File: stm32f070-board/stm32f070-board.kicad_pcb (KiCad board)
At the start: 2 copper layers, 39 parts, among them J1 USB_B_Micro, J2 USB_B_Micro, J3 Conn_01x05_Male, SW1 SW_DPDT_x2, SW2 SW_Push, SW3 SW_Push, U1 CH340G, U2 STM32F070F6P6, U3 MCP9700AT-ETT, U4 Si7055-A20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

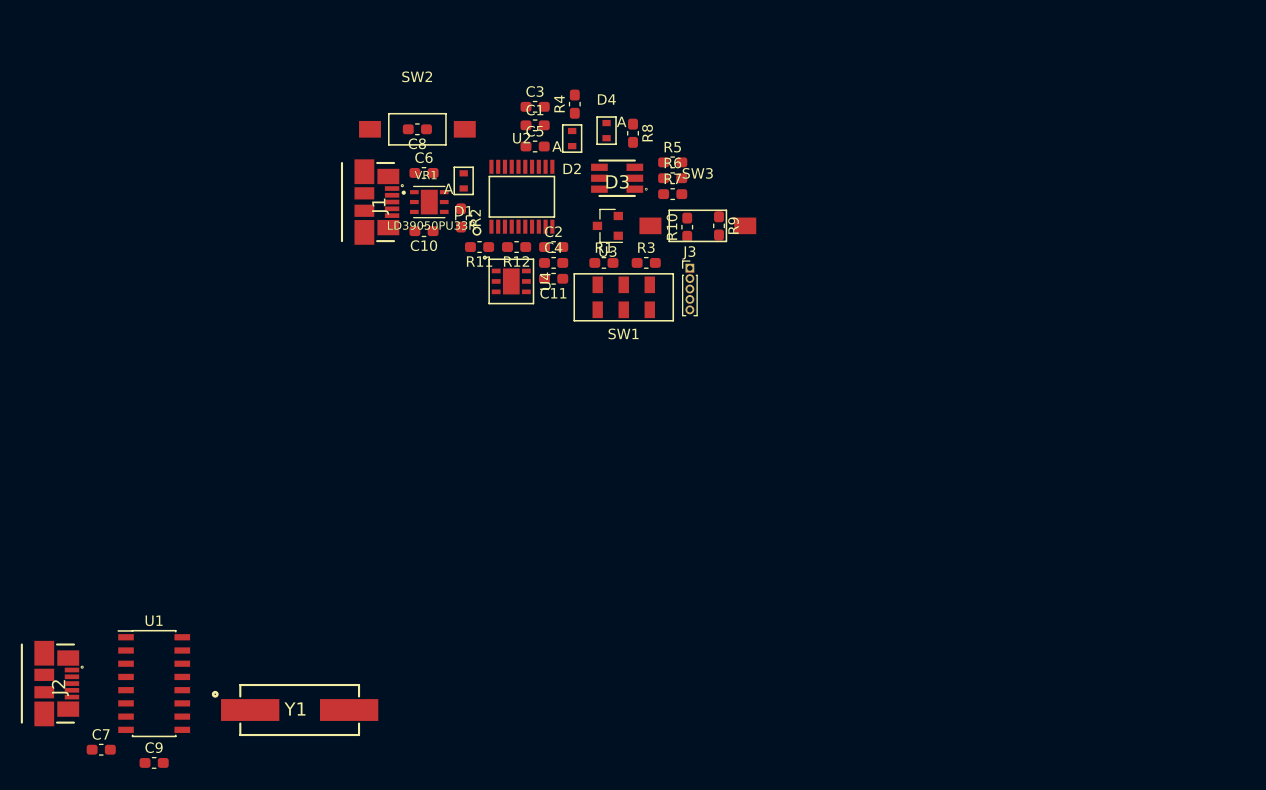
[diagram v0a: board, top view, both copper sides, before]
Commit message: laid out board on single side, changed the net name to match differential signal conventions in schematic
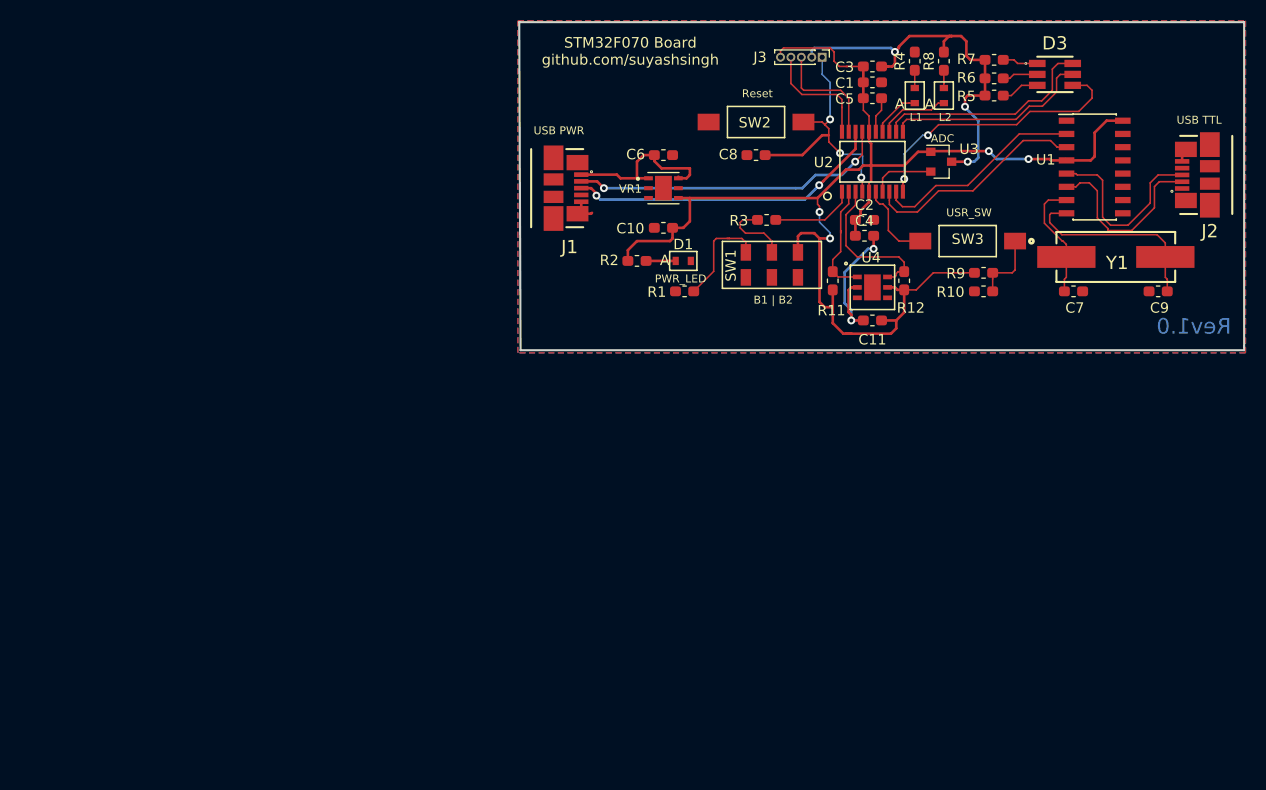
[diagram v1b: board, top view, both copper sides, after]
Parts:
- moved J2 126.0 mm to (163.2, 102.3), turned to 270 degrees
- moved C9 106.5 mm to (156.1, 113.5), turned to 180 degrees
- moved C7 103.2 mm to (148.0, 113.5)
- moved U1 103.0 mm to (150.0, 101.5)
- moved Y1 89.6 mm to (152.0, 110.2)
- moved D3 43.2 mm to (146.2, 92.6), turned to 0 degrees
- moved R12 37.4 mm to (131.7, 112.5), turned to 90 degrees
- moved U4 34.7 mm to (128.7, 113.1)
- moved R11 34.1 mm to (124.8, 112.5), turned to 90 degrees
- moved U2 33.8 mm to (128.7, 101.0)
- moved R7 33.4 mm to (140.3, 91.2), turned to 180 degrees
- moved D2 33.2 mm to (132.7, 94.7)
- moved R4 32.9 mm to (132.7, 91.4)
- moved C5 32.7 mm to (128.7, 94.9)
- moved C1 32.6 mm to (128.7, 93.4)
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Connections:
- net /USB_DM renamed /USB_D-
- net /USB_DP renamed /USB_D+
- net Net-(J2-Pad2) renamed /USB_Data-
- net Net-(J2-Pad3) renamed /USB_Data+
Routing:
- net VCC: track 0.00 -> 128.4 mm, vias 0 -> 4
- net GND: track 0.00 -> 61.4 mm, vias 0 -> 5
- net /USB_D-: track 0.00 -> 30.8 mm, vias 0 -> 2
- net /USB_D+: track 0.00 -> 30.6 mm, vias 0 -> 2
- net Net-(D3-Pad4): track 0.00 -> 26.7 mm, vias 0 -> 2
- net /ToDebugConnector: track 0.00 -> 25.2 mm, vias 0 -> 3
- net /TXD_uC: track 0.00 -> 21.6 mm
- net Net-(D3-Pad6): track 0.00 -> 21.4 mm
- net /RXD_uC: track 0.00 -> 20.3 mm
- net Net-(D3-Pad5): track 0.00 -> 19.8 mm
- net Net-(C9-Pad1): track 0.00 -> 19.1 mm
- net /USB_Data+: track 0.00 -> 18.4 mm
- net /USB_Data-: track 0.00 -> 17.9 mm
- net Net-(C6-Pad1): track 0.00 -> 16.4 mm
- net /SCL: track 0.00 -> 14.6 mm
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- added copper zone on B.Cu, net GND
- added copper zone on F.Cu, net GND
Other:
- board outline added: 69.6 x 31.5 mm
- board text added: "ADC"
- board text added: "B1 | B2"
- board text added: "L1"
- board text added: "L2"
- board text added: "PWR_LED"
- board text added: "Reset"
- board text added: "Rev1.0"
- board text added: "STM32F070 Board github.com/suyashsingh"
- board text added: "USB PWR"
- board text added: "USB TTL"
- board text added: "USR_SW"

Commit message: made final cosmetic changes to the pcb
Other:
- board text added: "PWR"
- board text added: "RGB LED"
- board text added: "STM32F070 Dev Kit"
- board text added: "Suyash Singh https://suyashsingh.github.io/"
- board text removed: "PWR_LED"
- board text removed: "STM32F070 Board github.com/suyashsingh"
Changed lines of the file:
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@@
-(kicad_pcb (version 20171130) (host pcbnew "(5.0.1)-3")
+(kicad_pcb (version 20171130) (host pcbnew 5.0.2-bee76a0~70~ubuntu18.04.1)
   (general
     (thickness 1.6)
-    (drawings 16)
+    (drawings 18)
     (tracks 397)
     (zones 0)
@@
   )
   (layers
-    (0 F.Cu signal hide)
+    (0 F.Cu signal)
     (31 B.Cu signal hide)
     (32 B.Adhes user hide)
@@
     (34 B.Paste user hide)
     (35 F.Paste user hide)
-    (36 B.SilkS user)
-    (37 F.SilkS user)
+    (36 B.SilkS user hide)
+    (37 F.SilkS user hide)
     (38 B.Mask user hide)
     (39 F.Mask user hide)
@@
     (42 Eco1.User user hide)
     (43 Eco2.User user hide)
-    (44 Edge.Cuts user)
+    (44 Edge.Cuts user hide)
     (45 Margin user hide)
-    (46 B.CrtYd user)
-    (47 F.CrtYd user)
+    (46 B.CrtYd user hide)
+    (47 F.CrtYd user hide)
     (48 B.Fab user hide)
     (49 F.Fab user hide)
   )
   (setup
-    (last_trace_width 0.1524)
+    (last_trace_width 0.254)
     (user_trace_width 0.1524)
     (trace_clearance 0.254)
@@
       (effects (font (size 1 1) (thickness 0.15)))
     )
-    (fp_text value Conn_01x05_Male (at 0 5.56 270) (layer F.Fab)
+    (fp_text value Conn_01x05_Male (at -0.0635 11.557) (layer F.Fab)
       (effects (font (size 1 1) (thickness 0.15)))
     )
@@
     (tags "capacitor handsolder")
     (attr smd)
-    (fp_text reference C2 (at 0 -1.43) (layer F.SilkS)
+    (fp_text reference C2 (at -2.667 0.0635) (layer F.SilkS)
       (effects (font (size 1 1) (thickness 0.15)))
     )
@@
     (tags "capacitor handsolder")
     (attr smd)
-    (fp_text reference C4 (at 0 -1.43) (layer F.SilkS)
+    (fp_text reference C4 (at -2.667 0.0635) (layer F.SilkS)
       (effects (font (size 1 1) (thickness 0.15)))
     )
@@
   (module stm32f070-board:LED_VISHAY (layer F.Cu)
     (at 110.49 110.5535 90)
-    (fp_text reference D1 (at 1.5875 0 180) (layer F.SilkS)
+    (fp_text reference D1 (at 0.0635 2.286 180) (layer F.Fab)
       (effects (font (size 1 1) (thickness 0.15)))
     )
@@
     (tags LED)
     (attr smd)
-    (fp_text reference D3 (at -0.019 -2.9845) (layer F.SilkS)
+    (fp_text reference D3 (at 4.445 0.0635) (layer F.Fab) hide
       (effects (font (size 1.27 1.27) (thickness 0.254)))
     )
-    (fp_text value LED_RGB (at -0.019 -0.396) (layer F.Fab) hide
+    (fp_text value LED_RGB (at 0.127 -2.9845) (layer F.Fab) hide
       (effects (font (size 1.27 1.27) (thickness 0.254)))
     )
@@
       (effects (font (size 1.27 1.27) (thickness 0.254)))
     )
-    (fp_text value USB_B_Micro (at -0.313 3.58 90) (layer F.Fab) hide
+    (fp_text value USB_B_Micro (at -5.6515 2.413 180) (layer F.Fab) hide
       (effects (font (size 1.27 1.27) (thickness 0.254)))
     )
@@
     (tags "resistor handsolder")
     (attr smd)
-    (fp_text reference R4 (at 0 -1.43 90) (layer F.SilkS)
+    (fp_text reference R4 (at 2.2225 0.127 180) (layer F.SilkS)
       (effects (font (size 1 1) (thickness 0.15)))
     )
@@
     (tags "resistor handsolder")
     (attr smd)
-    (fp_text reference R8 (at 0 -1.43 270) (layer F.SilkS)
+    (fp_text reference R8 (at 2.2225 0.127) (layer F.SilkS)
       (effects (font (size 1 1) (thickness 0.15)))
     )
@@
       (net 6 "Net-(C9-Pad1)"))
   )
+  (gr_text "Suyash Singh\nhttps://suyashsingh.github.io/" (at 145.542 92.202) (layer B.SilkS)
+    (effects (font (size 1.5 1.5) (thickness 0.3)) (justify mirror))
+  )
+  (gr_text "RGB LED\n" (at 146.304 89.662) (layer F.SilkS)
+    (effects (font (size 0.762 0.762) (thickness 0.1524)))
+  )
   (gr_text "B1 | B2" (at 119.126 114.3) (layer F.SilkS)
     (effects (font (size 0.762 0.762) (thickness 0.1524)))
@@
     (effects (font (size 0.762 0.762) (thickness 0.1524)))
   )
-  (gr_text PWR_LED (at 110.236 112.268) (layer F.SilkS)
+  (gr_text "PWR\n" (at 110.49 108.966) (layer F.SilkS)
     (effects (font (size 0.762 0.762) (thickness 0.1524)))
   )
@@
     (effects (font (size 0.762 0.762) (thickness 0.1524)))
   )
-  (gr_text "STM32F070 Board\ngithub.com/suyashsingh" (at 105.41 90.424) (layer F.SilkS)
+  (gr_text "STM32F070 Dev Kit\n\n" (at 104.14 92.202) (layer F.SilkS)
     (effects (font (size 1.016 1.016) (thickness 0.1524)))
   )

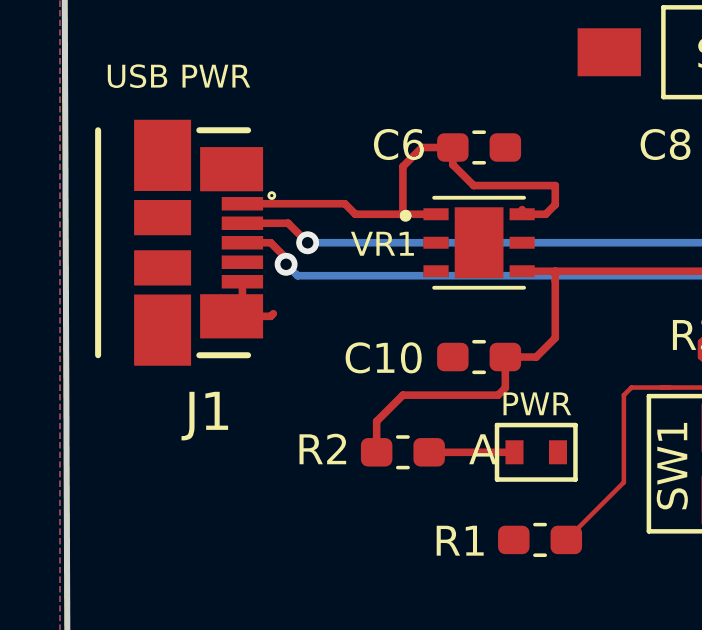
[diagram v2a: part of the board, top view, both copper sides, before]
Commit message: Removed stray ground trace near the usb jack
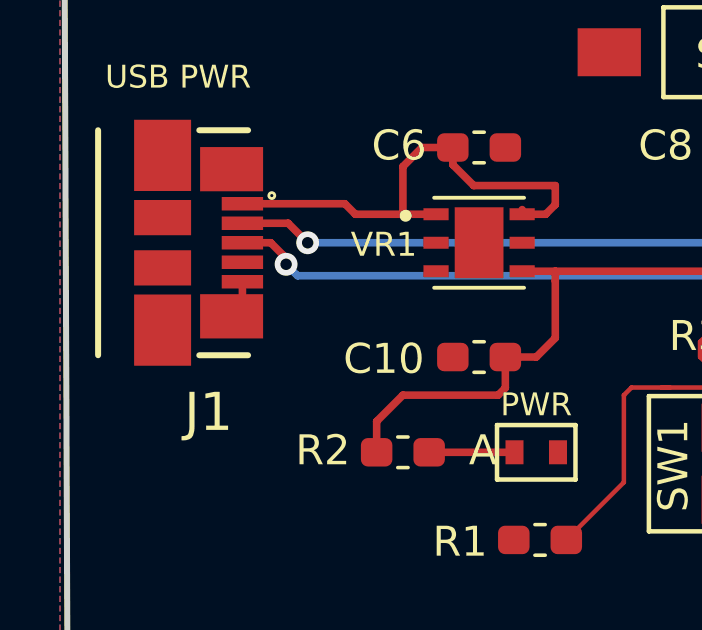
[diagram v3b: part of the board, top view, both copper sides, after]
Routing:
- net GND: track 61.4 -> 60.0 mm
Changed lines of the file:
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@@
-(kicad_pcb (version 20171130) (host pcbnew 5.0.2-bee76a0~70~ubuntu18.04.1)
+(kicad_pcb (version 20171130) (host pcbnew "(5.0.1)-3")
   (general
     (thickness 1.6)
     (drawings 18)
-    (tracks 397)
+    (tracks 395)
     (zones 0)
     (modules 39)
@@
   (segment (start 137.16 88.9635) (end 136.271 88.9635) (width 0.254) (layer F.Cu) (net 2))
   (segment (start 136.271 88.9635) (end 136.017 88.9635) (width 0.254) (layer F.Cu) (net 2))
-  (segment (start 101.639 106.021) (end 101.727 105.933) (width 0.254) (layer F.Cu) (net 2))
-  (segment (start 100.335 106.021) (end 101.639 106.021) (width 0.254) (layer F.Cu) (net 2))
   (segment (start 100.695 105.661) (end 100.335 106.021) (width 0.254) (layer F.Cu) (net 2))
   (segment (start 100.695 104.8685) (end 100.695 105.661) (width 0.254) (layer F.Cu) (net 2))
